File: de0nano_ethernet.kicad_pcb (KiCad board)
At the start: 2 copper layers, 19 x 55.9 mm, 3 parts

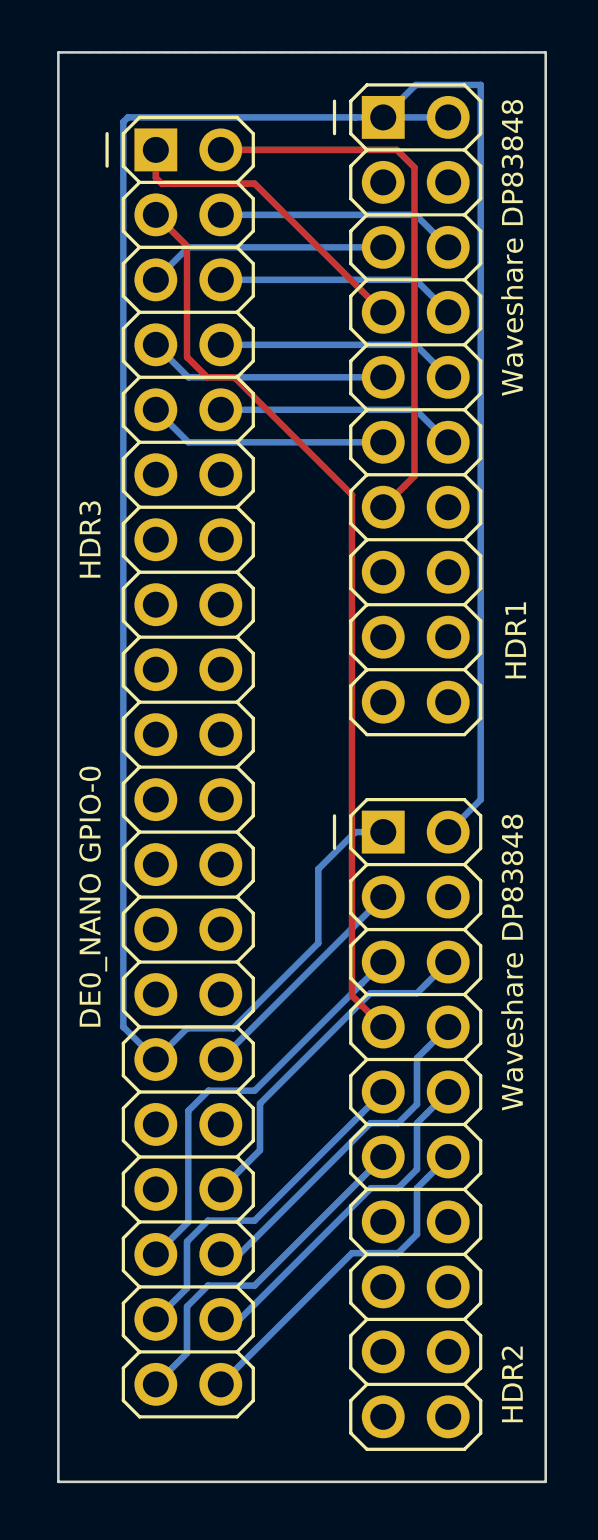
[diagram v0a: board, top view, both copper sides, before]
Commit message: add version and designer to silkscreen
create gerber files and zip file for osk park
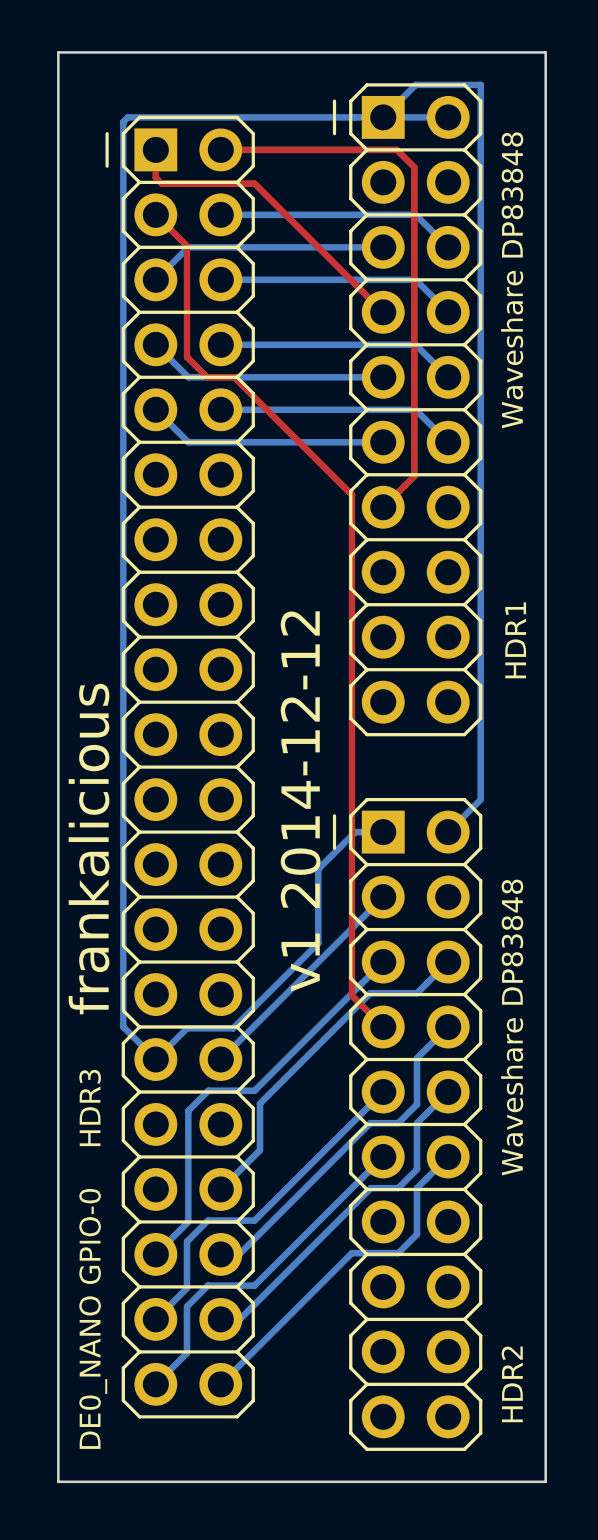
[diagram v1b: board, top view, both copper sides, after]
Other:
- board text added: "frankalicious"
- board text added: "v1 2014-12-12"
